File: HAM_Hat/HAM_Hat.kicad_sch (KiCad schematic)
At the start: 62 parts, among them J101 TL212V-02P-G12S, J102 DB-9RS-C, J103 NCW254-02S, J104 SMA6252A2, J105 NCW200S-04R, J106 Conn_01x02, J3 FHDH2.54-40, M101 Fan, Q101 BSS138, Q102 BSS138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

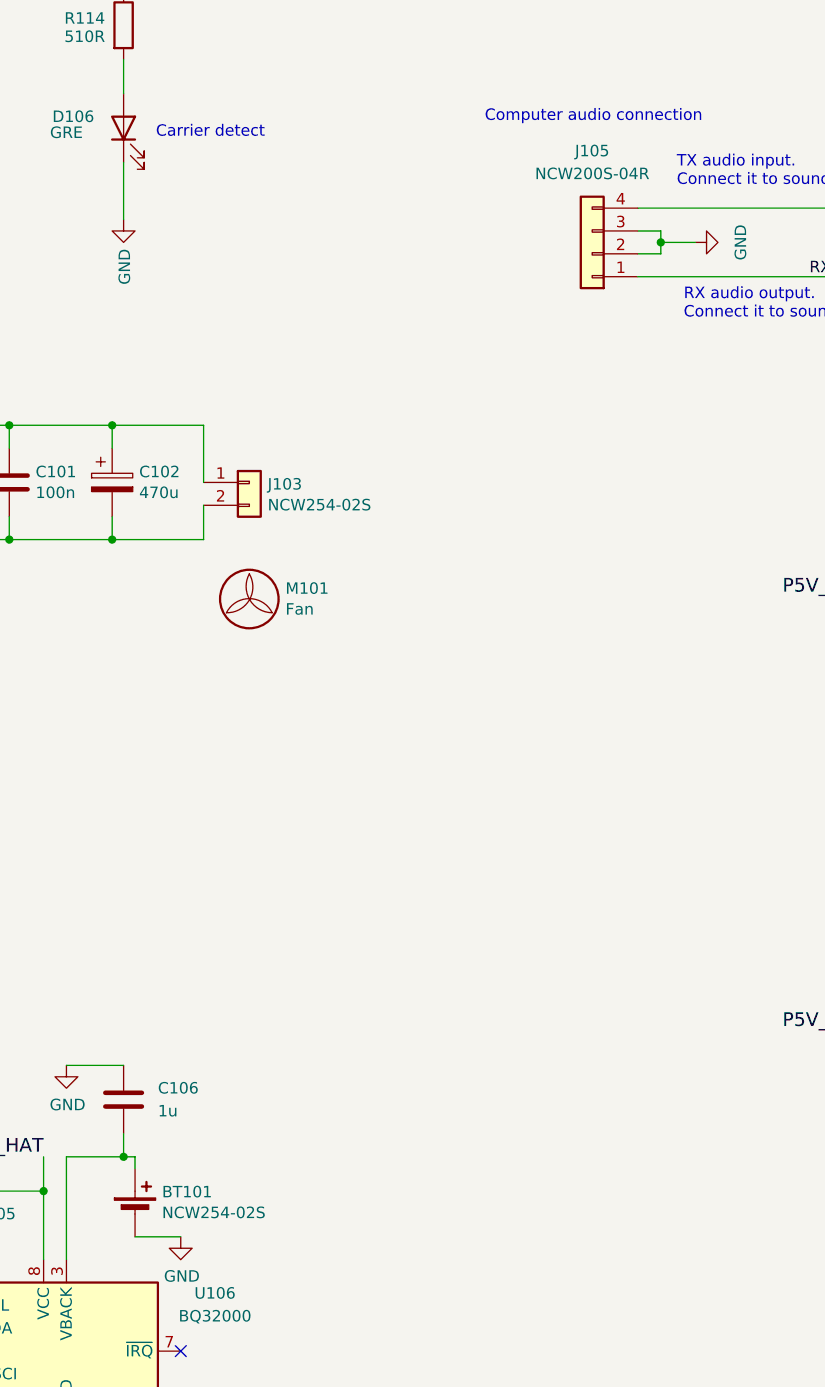
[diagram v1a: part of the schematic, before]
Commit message: Replace the 2mm pitch connector to 2.54mm pitch
This is not really a connector, rather then a pads to
solder wires.
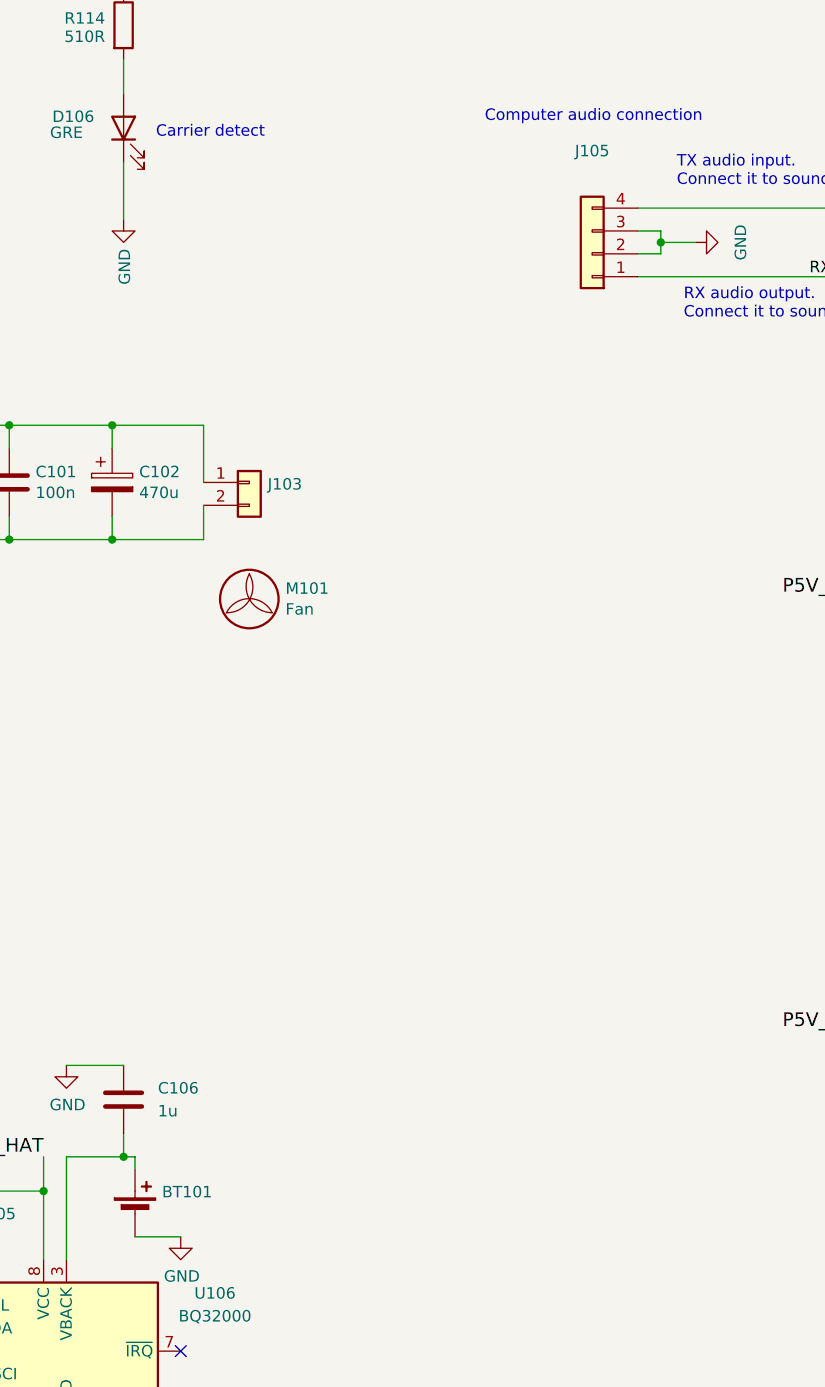
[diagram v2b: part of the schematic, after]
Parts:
- BT101, J103: value NCW254-02S -> (none)
- J105: value NCW200S-04R -> ~; footprint Connector_JST:JST_PH_B4B-PH-K_1x04_P2.00mm_Vertical -> Connector_PinHeader_2.54mm:PinHeader_1x04_P2.54mm_Vertical; id 459 -> 0
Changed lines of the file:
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@@
 			)
 		)
-		(property "Value" "NCW254-02S"
+		(property "Value" ""
 			(at 207.772 159.9946 0)
 			(effects
@@
 			)
 		)
-		(property "Value" "NCW254-02S"
+		(property "Value" ""
 			(at 196.0372 238.633 0)
 			(effects
@@
 			)
 		)
-		(property "Value" "NCW200S-04R"
+		(property "Value" "~"
 			(at 243.84 123.19 0)
 			(effects
@@
 			)
 		)
-		(property "Footprint" "Connector_JST:JST_PH_B4B-PH-K_1x04_P2.00mm_Vertical"
+		(property "Footprint" "Connector_PinHeader_2.54mm:PinHeader_1x04_P2.54mm_Vertical"
 			(at 243.84 132.08 0)
 			(effects
@@
 			)
 		)
-		(property "id" "459"
+		(property "id" "0"
 			(at 243.84 132.08 0)
 			(effects

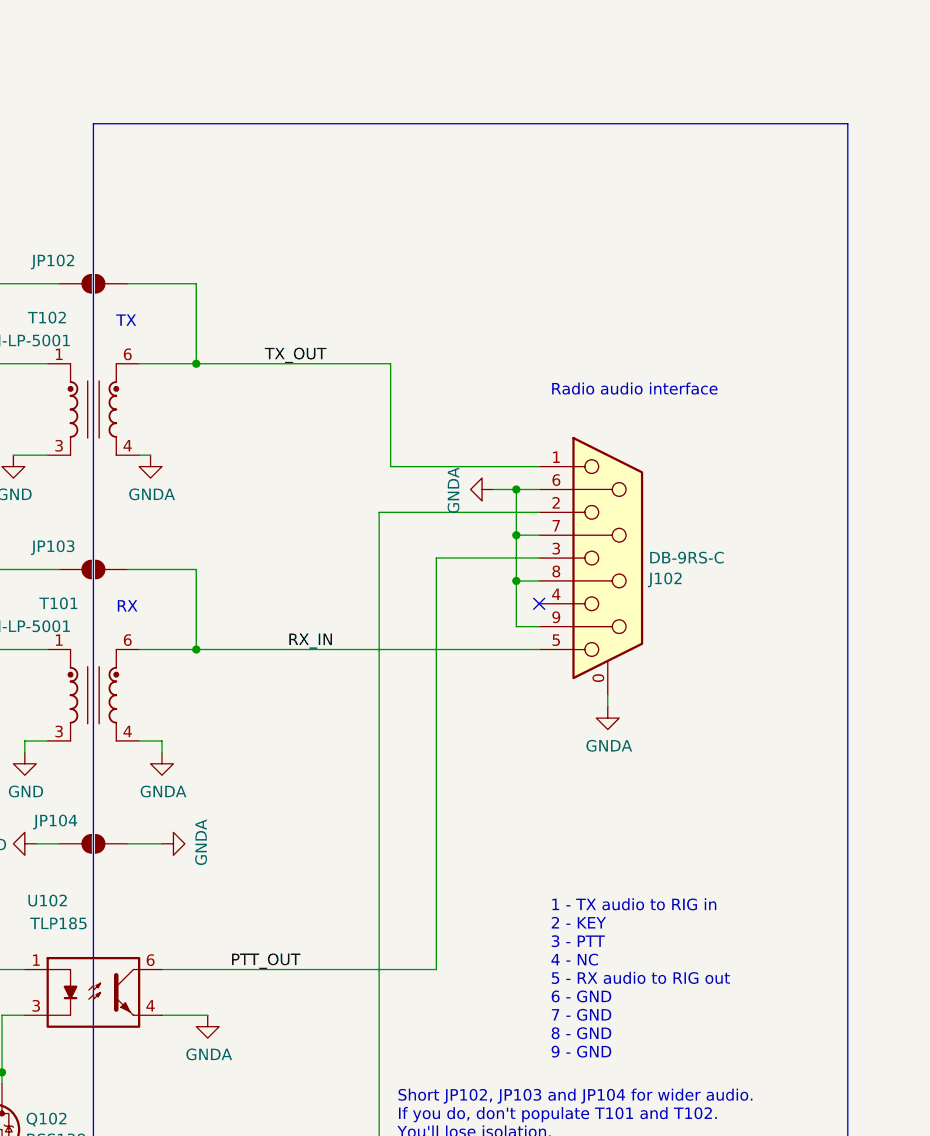
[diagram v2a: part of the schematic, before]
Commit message: Add HT radio option
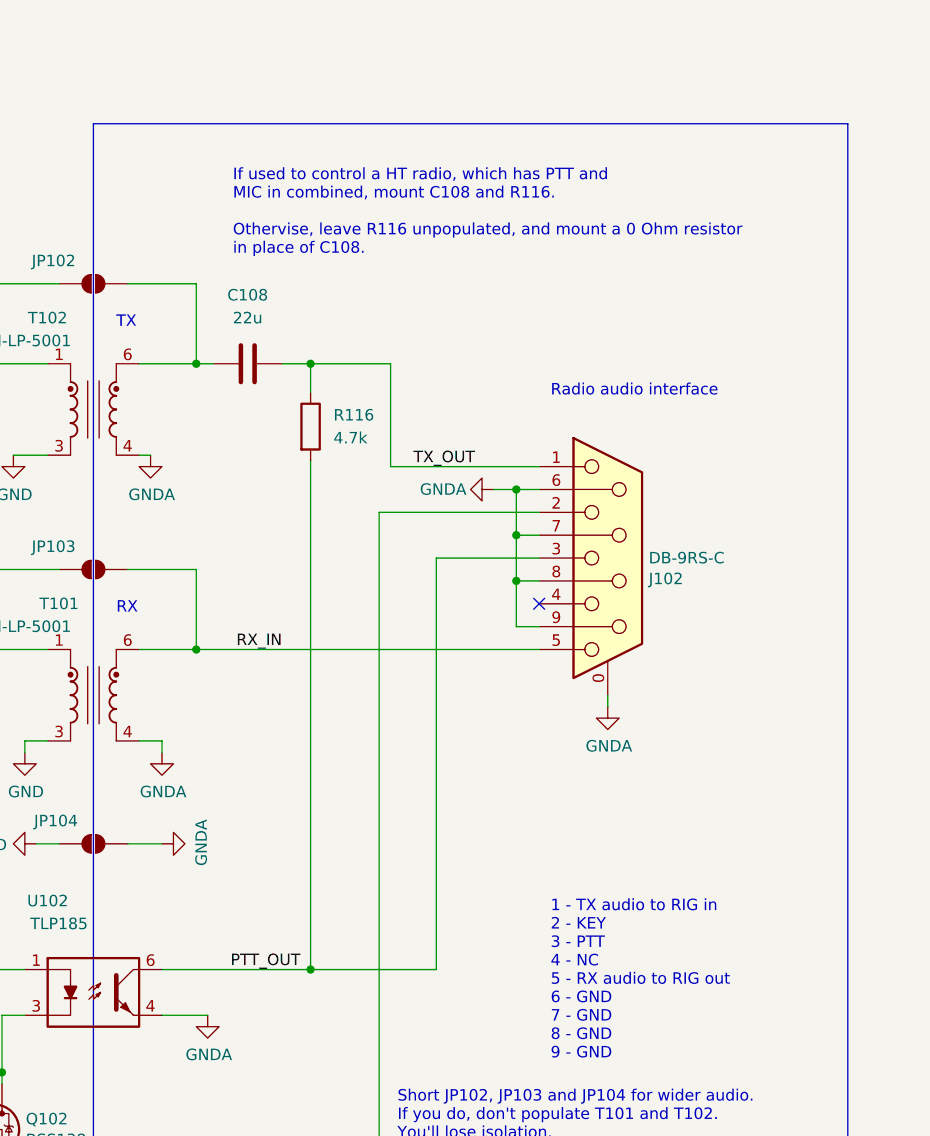
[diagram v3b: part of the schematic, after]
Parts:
- added C108: 22u, Capacitor_SMD:C_1206_3216Metric, symbol default:levcsi_database/340
- added R116: 4.7k, Resistor_SMD:R_0603_1608Metric, symbol default:levcsi_database/253
- BT101, J103: value (none) -> ~
- J105: value ~ -> (none)
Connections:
- net PTT_OUT: now also R116.2
- net TX_OUT: now also C108.2, R116.1; no longer JP102.2 (B), T102.6
- new net: C108.1, JP102.2 (B), T102.6
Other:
- note added: "If used to control a HT radio, which has PTT and MIC in combined, mount C108 and R116. Othervise, leave R116 unpopulated, and mount a 0 Ohm resistor in place of C108."

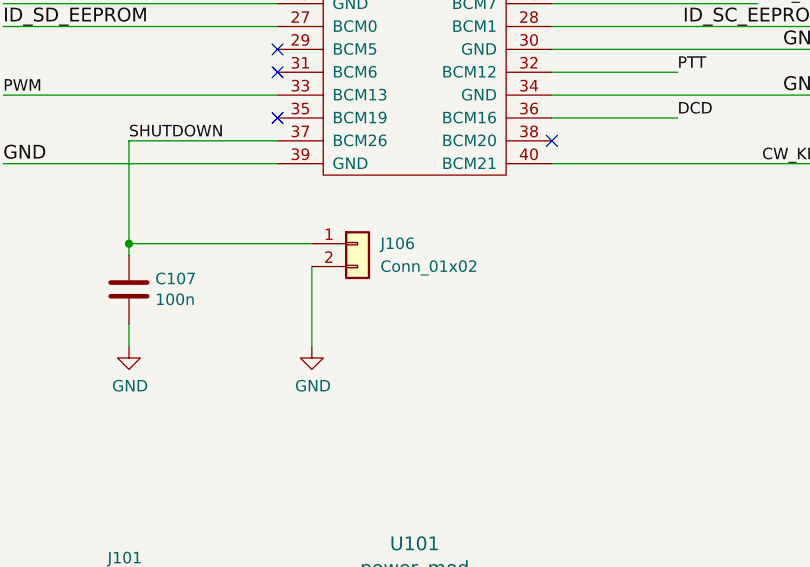
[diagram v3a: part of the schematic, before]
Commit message: Move shutdown connector
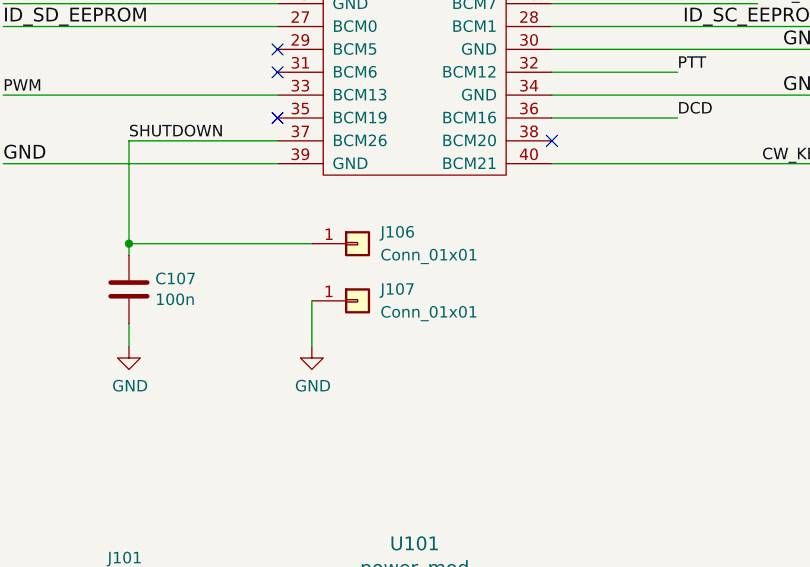
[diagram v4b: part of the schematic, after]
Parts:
- removed J106: Conn_01x02, Connector_Wire:SolderWire-0.5sqmm_1x02_P4.6mm_D0.9mm_OD2.1mm, symbol Connector_Generic:Conn_01x02
- added J106, J107: Conn_01x01, l_connector:SolderWirePad_1x01_SMD_2x5mm, symbol Connector_Generic:Conn_01x01
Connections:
- net GND: now also J107.1 (Pin_1)
- net SHUTDOWN: now also J106.1 (Pin_1)
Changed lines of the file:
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@@
 	(wire
 		(pts
+			(xy 54.61 120.65) (xy 54.61 125.73)
+		)
+		(stroke
+			(width 0)
+			(type default)
+		)
+	)
+	(wire
+		(pts
 			(xy 318.77 146.05) (xy 318.77 144.78)
 		)
@@
 	(wire
 		(pts
-			(xy 54.61 116.84) (xy 54.61 125.73)
-		)
-		(stroke
-			(width 0)
-			(type default)
-		)
-	)
-	(wire
-		(pts
 			(xy 285.75 181.61) (xy 278.13 181.61)
 		)
@@
 	)
 	(symbol
-		(lib_id "Connector_Generic:Conn_01x02")
-		(at 59.69 114.3 0)
-		(unit 1)
-		(exclude_from_sim no)
-		(in_bom yes)
-		(on_board yes)
-		(dnp no)
-		(fields_autoplaced yes)
-		(property "Reference" "J106"
-			(at 62.23 114.2999 0)
-			(effects
-				(font
-					(size 1.27 1.27)
-				)
-				(justify left)
-			)
-		)
-		(property "Value" "Conn_01x02"
-			(at 62.23 116.8399 0)
-			(effects
-				(font
-					(size 1.27 1.27)
-				)
-				(justify left)
-			)
-		)
-		(property "Footprint" "Connector_Wire:SolderWire-0.5sqmm_1x02_P4.6mm_D0.9mm_OD2.1mm"
-			(at 59.69 114.3 0)
-			(effects
-				(font
-					(size 1.27 1.27)
-				)
-				(hide yes)
-			)
-		)
-		(property "Datasheet" "~"
-			(at 59.69 114.3 0)
-			(effects
-				(font
-					(size 1.27 1.27)
-				)
-				(hide yes)
-			)
-		)
-		(property "Description" "Generic connector, single row, 01x02, script generated (kicad-library-utils/schlib/autogen/connector/)"
-			(at 59.69 114.3 0)
-			(effects
-				(font
-					(size 1.27 1.27)
-				)
-				(hide yes)
-			)
-		)
-		(pin "1"
-		)
-		(pin "2"
-		)
-		(instances
-			(project ""
-				(path "/d746ec70-4f38-4eaf-8576-334127e7f74a"
-					(reference "J106")
-					(unit 1)
-				)
-			)
-		)
-	)
-	(symbol
 		(lib_id "Device:R")
 		(at 191.77 106.68 0)
@@
 	)
 	(symbol
+		(lib_id "Connector_Generic:Conn_01x01")
+		(at 59.69 120.65 0)
+		(unit 1)
+		(exclude_from_sim no)
+		(in_bom yes)
+		(on_board yes)
+		(dnp no)
+		(fields_autoplaced yes)
+		(property "Reference" "J107"
+			(at 62.23 119.3799 0)
+			(effects
+				(font
+					(size 1.27 1.27)
+				)
+				(justify left)
+			)
+		)
+		(property "Value" "Conn_01x01"
+			(at 62.23 121.9199 0)
+			(effects
+				(font
+					(size 1.27 1.27)
+				)
+				(justify left)
+			)
+		)
+		(property "Footprint" "l_connector:SolderWirePad_1x01_SMD_2x5mm"
+			(at 59.69 120.65 0)
+			(effects
+				(font
+					(size 1.27 1.27)
+				)
+				(hide yes)
+			)
+		)
+		(property "Datasheet" "~"
+			(at 59.69 120.65 0)
+			(effects
+				(font
+					(size 1.27 1.27)
+				)
+				(hide yes)
+			)
+		)
+		(property "Description" "Generic connector, single row, 01x01, script generated (kicad-library-utils/schlib/autogen/connector/)"
+			(at 59.69 120.65 0)
+			(effects
+				(font
+					(size 1.27 1.27)
+				)
+				(hide yes)
+			)
+		)
+		(pin "1"
+		)
+		(instances
+			(project "HAM_Hat"
+				(path "/d746ec70-4f38-4eaf-8576-334127e7f74a"
+					(reference "J107")
+					(unit 1)
+				)
+			)
+		)
+	)
+	(symbol
 		(lib_id "Timer_RTC:BQ32000")
 		(at 185.42 254 0)
@@
 					(unit 1)
 				)
+			)
+		)
+	)
+	(symbol
+		(lib_id "Connector_Generic:Conn_01x01")
+		(at 59.69 114.3 0)
+		(unit 1)
+		(exclude_from_sim no)
+		(in_bom yes)
+		(on_board yes)
+		(dnp no)
+		(fields_autoplaced yes)
+		(property "Reference" "J106"
+			(at 62.23 113.0299 0)
+			(effects
+				(font
+					(size 1.27 1.27)
+				)
+				(justify left)
+			)
+		)
+		(property "Value" "Conn_01x01"
+			(at 62.23 115.5699 0)
+			(effects
+				(font
+					(size 1.27 1.27)
+				)
+				(justify left)
+			)
+		)
+		(property "Footprint" "l_connector:SolderWirePad_1x01_SMD_2x5mm"
+			(at 59.69 114.3 0)
+			(effects
+				(font
+					(size 1.27 1.27)
+				)
+				(hide yes)
+			)
+		)
+		(property "Datasheet" "~"
+			(at 59.69 114.3 0)
+			(effects
+				(font
+					(size 1.27 1.27)
+				)
+				(hide yes)
+			)
+		)
+		(property "Description" "Generic connector, single row, 01x01, script generated (kicad-library-utils/schlib/autogen/connector/)"
+			(at 59.69 114.3 0)
+			(effects
+				(font
+					(size 1.27 1.27)
+				)
+				(hide yes)
+			)
+		)
+		(pin "1"
+		)
+		(instances
+			(project ""
+				(path "/d746ec70-4f38-4eaf-8576-334127e7f74a"
+					(reference "J106")
+					(unit 1)
+				)
